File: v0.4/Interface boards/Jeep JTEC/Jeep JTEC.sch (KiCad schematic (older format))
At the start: 8 parts, among them J1 Conn_02x20_Counter_Clockwise

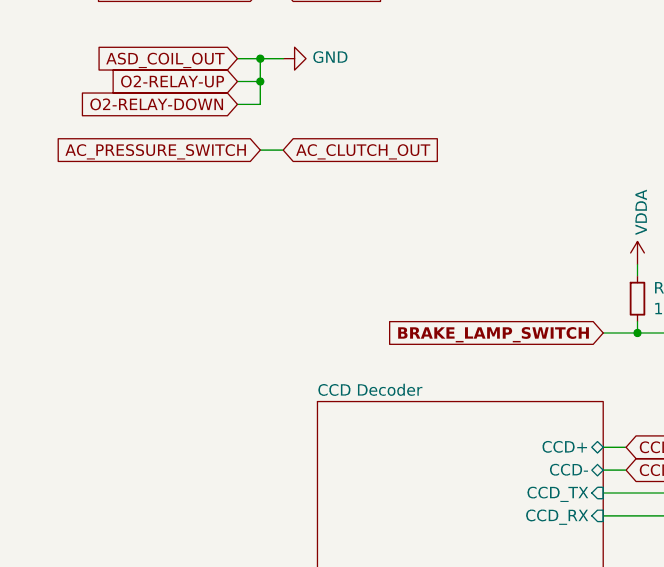
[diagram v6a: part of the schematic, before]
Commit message: Add jumper for GND and GNDA. Add 12v-SW output
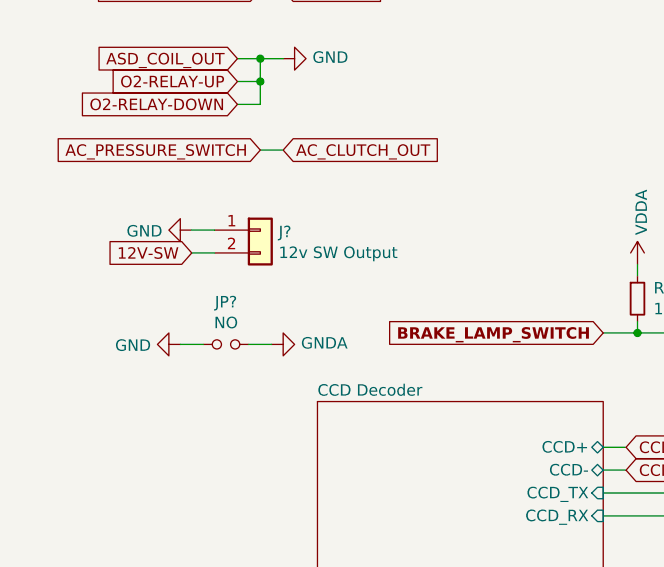
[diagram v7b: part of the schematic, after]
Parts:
- added J?: 12v SW Output, symbol Connector_Generic:Conn_01x02
- added JP?: NO, Connector_PinHeader_2.54mm:PinHeader_1x02_P2.54mm_Vertical, symbol Device:Jumper_NO_Small
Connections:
- net 12V-SW: now also J?.2 (Pin_2)
- net GND: now also J?.1 (Pin_1), JP?.1
- net GNDA: now also JP?.2
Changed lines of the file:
@@
 EESchema Schematic File Version 4
-LIBS:Jeep JTEC-cache
 EELAYER 30 0
 EELAYER END
@@
 Text GLabel 7100 6300 2    50   Input ~ 0
 ASD_12V_IN
+$Comp
+L Connector_Generic:Conn_01x02 J?
+U 1 1 61A64B30
+P 1450 5250
+F 0 "J?" H 1530 5242 50  0000 L CNN
+F 1 "12v SW Output" H 1530 5151 50  0000 L CNN
+F 2 "" H 1450 5250 50  0001 C CNN
+F 3 "~" H 1450 5250 50  0001 C CNN
+	1    1450 5250
+	1    0    0    -1
+$EndComp
+Wire Wire Line
+	1250 5250 1150 5250
+Wire Wire Line
+	1250 5350 1150 5350
+$Comp
+L power:GND #PWR?
+U 1 1 61A7A083
+P 1150 5250
+F 0 "#PWR?" H 1150 5000 50  0001 C CNN
+F 1 "GND" V 1155 5122 50  0000 R CNN
+F 2 "" H 1150 5250 50  0001 C CNN
+F 3 "" H 1150 5250 50  0001 C CNN
+	1    1150 5250
+	0    1    1    0
+$EndComp
+Text GLabel 1150 5350 0    50   Input ~ 0
+12V-SW
+$Comp
+L Device:Jumper_NO_Small JP?
+U 1 1 61A8768C
+P 1300 5750
+F 0 "JP?" H 1300 5935 50  0000 C CNN
+F 1 "NO" H 1300 5844 50  0000 C CNN
+F 2 "Connector_PinHeader_2.54mm:PinHeader_1x02_P2.54mm_Vertical" H 1300 5750 50  0001 C CNN
+F 3 "~" H 1300 5750 50  0001 C CNN
+F 4 "10129378-902001BLF" H 1300 5750 50  0001 C CNN "Manufacturer"
+F 5 "Amphenol ICC (FCI)" H 1300 5750 50  0001 C CNN "Manufacturer#"
+F 6 "10129378-902001BLF-ND" H 1300 5750 50  0001 C CNN "digikey#"
+	1    1300 5750
+	1    0    0    -1
+$EndComp
+Wire Wire Line
+	1100 5750 1200 5750
+Wire Wire Line
+	1400 5750 1500 5750
+$Comp
+L power:GND #PWR?
+U 1 1 61A9CEE4
+P 1100 5750
+F 0 "#PWR?" H 1100 5500 50  0001 C CNN
+F 1 "GND" V 1105 5622 50  0000 R CNN
+F 2 "" H 1100 5750 50  0001 C CNN
+F 3 "" H 1100 5750 50  0001 C CNN
+	1    1100 5750
+	0    1    1    0
+$EndComp
+$Comp
+L power:GNDA #PWR?
+U 1 1 61A9D2A5
+P 1500 5750
+F 0 "#PWR?" H 1500 5500 50  0001 C CNN
+F 1 "GNDA" V 1505 5622 50  0000 R CNN
+F 2 "" H 1500 5750 50  0001 C CNN
+F 3 "" H 1500 5750 50  0001 C CNN
+	1    1500 5750
+	0    -1   -1   0
+$EndComp
 $EndSCHEMATC

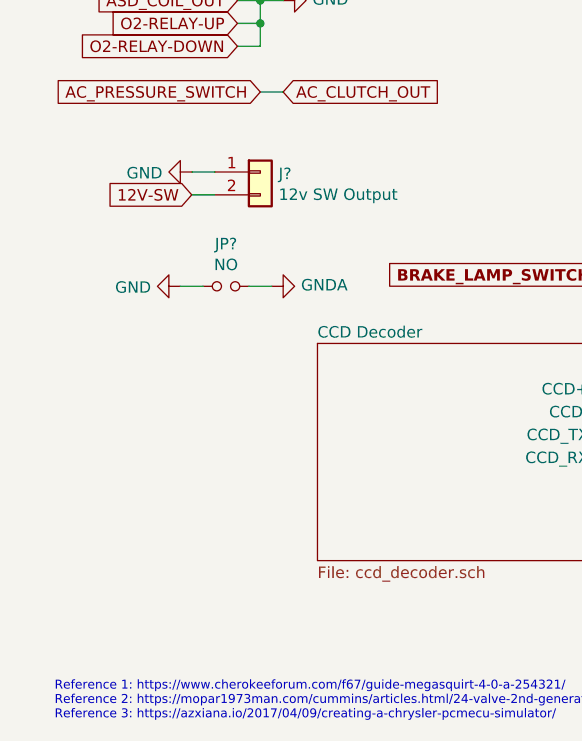
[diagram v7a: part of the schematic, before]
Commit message: Add 12v output to PCB
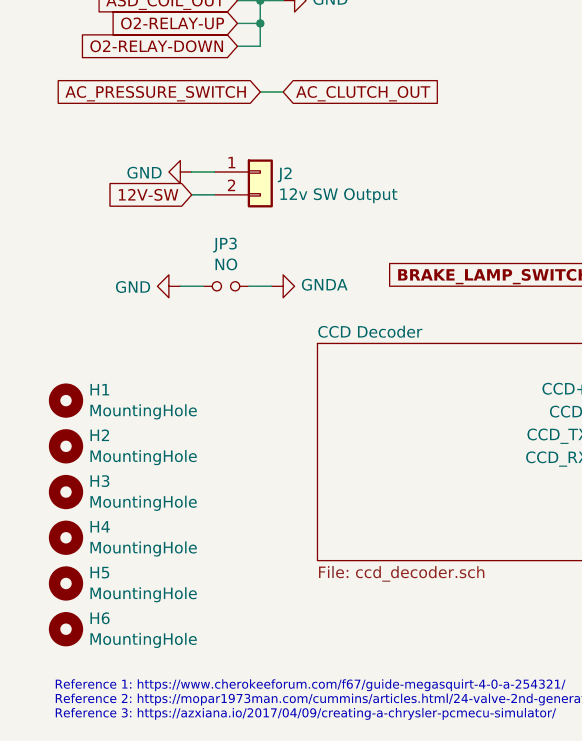
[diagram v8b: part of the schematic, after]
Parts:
- added H1, H2, H3, H4, H5, H6: MountingHole, MountingHole:MountingHole_4.3mm_M4_Pad_Via, symbol Mechanical:MountingHole
- J2: renamed from J?; footprint (none) -> Connector_Phoenix_MC:PhoenixContact_MCV_1,5_2-GF-3.81_1x02_P3.81mm_Vertical_ThreadedFlange_MountHole
- gave numbers to parts that had none: 1
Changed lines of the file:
@@
 ASD_12V_IN
 $Comp
-L Connector_Generic:Conn_01x02 J?
+L Connector_Generic:Conn_01x02 J2
 U 1 1 61A64B30
 P 1450 5250
-F 0 "J?" H 1530 5242 50  0000 L CNN
+F 0 "J2" H 1530 5242 50  0000 L CNN
 F 1 "12v SW Output" H 1530 5151 50  0000 L CNN
-F 2 "" H 1450 5250 50  0001 C CNN
+F 2 "Connector_Phoenix_MC:PhoenixContact_MCV_1,5_2-GF-3.81_1x02_P3.81mm_Vertical_ThreadedFlange_MountHole" H 1450 5250 50  0001 C CNN
 F 3 "~" H 1450 5250 50  0001 C CNN
 	1    1450 5250
@@
 	1250 5350 1150 5350
 $Comp
-L power:GND #PWR?
+L power:GND #PWR0101
 U 1 1 61A7A083
 P 1150 5250
-F 0 "#PWR?" H 1150 5000 50  0001 C CNN
+F 0 "#PWR0101" H 1150 5000 50  0001 C CNN
 F 1 "GND" V 1155 5122 50  0000 R CNN
 F 2 "" H 1150 5250 50  0001 C CNN
@@
 12V-SW
 $Comp
-L Device:Jumper_NO_Small JP?
+L Device:Jumper_NO_Small JP3
 U 1 1 61A8768C
 P 1300 5750
-F 0 "JP?" H 1300 5935 50  0000 C CNN
+F 0 "JP3" H 1300 5935 50  0000 C CNN
 F 1 "NO" H 1300 5844 50  0000 C CNN
 F 2 "Connector_PinHeader_2.54mm:PinHeader_1x02_P2.54mm_Vertical" H 1300 5750 50  0001 C CNN
@@
 	1400 5750 1500 5750
 $Comp
-L power:GND #PWR?
+L power:GND #PWR0102
 U 1 1 61A9CEE4
 P 1100 5750
-F 0 "#PWR?" H 1100 5500 50  0001 C CNN
+F 0 "#PWR0102" H 1100 5500 50  0001 C CNN
 F 1 "GND" V 1105 5622 50  0000 R CNN
 F 2 "" H 1100 5750 50  0001 C CNN
@@
 $EndComp
 $Comp
-L power:GNDA #PWR?
+L power:GNDA #PWR0103
 U 1 1 61A9D2A5
 P 1500 5750
-F 0 "#PWR?" H 1500 5500 50  0001 C CNN
+F 0 "#PWR0103" H 1500 5500 50  0001 C CNN
 F 1 "GNDA" V 1505 5622 50  0000 R CNN
 F 2 "" H 1500 5750 50  0001 C CNN
@@
 	0    -1   -1   0
 $EndComp
+$Comp
+L Mechanical:MountingHole H3
+U 1 1 615F1836
+P 600 6650
+F 0 "H3" H 700 6696 50  0000 L CNN
+F 1 "MountingHole" H 700 6605 50  0000 L CNN
+F 2 "MountingHole:MountingHole_4.3mm_M4_Pad_Via" H 600 6650 50  0001 C CNN
+F 3 "~" H 600 6650 50  0001 C CNN
+	1    600  6650
+	1    0    0    -1
+$EndComp
+$Comp
+L Mechanical:MountingHole H4
+U 1 1 615F1BA5
+P 600 6850
+F 0 "H4" H 700 6896 50  0000 L CNN
+F 1 "MountingHole" H 700 6805 50  0000 L CNN
+F 2 "MountingHole:MountingHole_4.3mm_M4_Pad_Via" H 600 6850 50  0001 C CNN
+F 3 "~" H 600 6850 50  0001 C CNN
+	1    600  6850
+	1    0    0    -1
+$EndComp
+$Comp
+L Mechanical:MountingHole H5
+U 1 1 615F1E09
+P 600 7050
+F 0 "H5" H 700 7096 50  0000 L CNN
+F 1 "MountingHole" H 700 7005 50  0000 L CNN
+F 2 "MountingHole:MountingHole_4.3mm_M4_Pad_Via" H 600 7050 50  0001 C CNN
+F 3 "~" H 600 7050 50  0001 C CNN
+	1    600  7050
+	1    0    0    -1
+$EndComp
+$Comp
+L Mechanical:MountingHole H6
+U 1 1 615F2008
+P 600 7250
+F 0 "H6" H 700 7296 50  0000 L CNN
+F 1 "MountingHole" H 700 7205 50  0000 L CNN
+F 2 "MountingHole:MountingHole_4.3mm_M4_Pad_Via" H 600 7250 50  0001 C CNN
+F 3 "~" H 600 7250 50  0001 C CNN
+	1    600  7250
+	1    0    0    -1
+$EndComp
+$Comp
+L Mechanical:MountingHole H2
+U 1 1 615F22EE
+P 600 6450
+F 0 "H2" H 700 6496 50  0000 L CNN
+F 1 "MountingHole" H 700 6405 50  0000 L CNN
+F 2 "MountingHole:MountingHole_4.3mm_M4_Pad_Via" H 600 6450 50  0001 C CNN
+F 3 "~" H 600 6450 50  0001 C CNN
+	1    600  6450
+	1    0    0    -1
+$EndComp
+$Comp
+L Mechanical:MountingHole H1
+U 1 1 615F25BB
+P 600 6250
+F 0 "H1" H 700 6296 50  0000 L CNN
+F 1 "MountingHole" H 700 6205 50  0000 L CNN
+F 2 "MountingHole:MountingHole_4.3mm_M4_Pad_Via" H 600 6250 50  0001 C CNN
+F 3 "~" H 600 6250 50  0001 C CNN
+	1    600  6250
+	1    0    0    -1
+$EndComp
 $EndSCHEMATC
